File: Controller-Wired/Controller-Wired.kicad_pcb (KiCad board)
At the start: 4 copper layers, 73.5 x 47.5 mm, 33 parts, among them J1 Conn_01x03, J2 Conn_02x20_Odd_Even, J3 Conn_01x06, J4 USB_C_Receptacle, SW1 SW_Push, U1 STM32F103CBTx, U2 AP131-33, U3 USBLC6-2SC6, Y1 Crystal

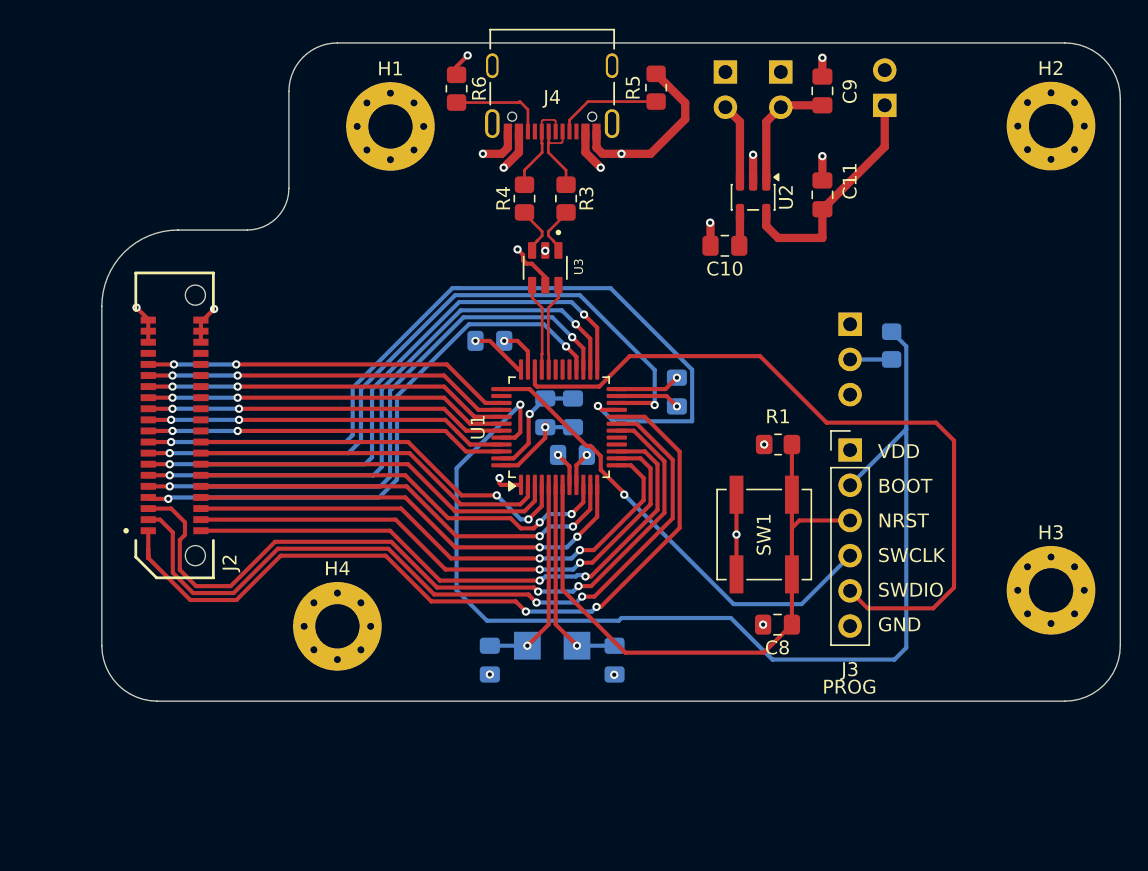
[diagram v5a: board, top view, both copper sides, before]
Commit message: USB connector was giving some net problems, swapped with a different one
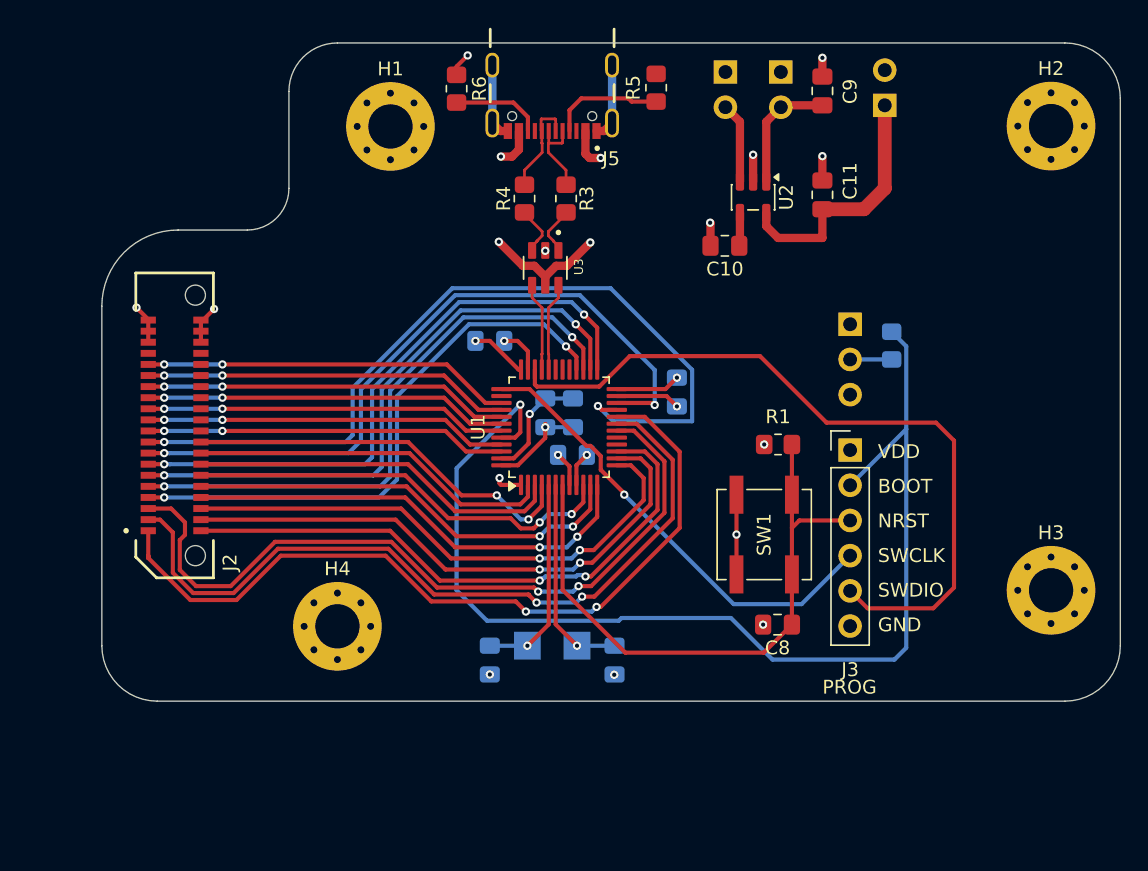
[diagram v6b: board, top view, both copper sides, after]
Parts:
- removed J4: USB_C_Receptacle, Controller:AMPHENOL_12402012E212A
- added J5: USB4105-GF-A, Controller:GCT_USB4105-GF-A, F.Cu at (124.0, 40.1)
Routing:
- net VBUS: track 9.77 -> 15.0 mm, vias 3 -> 4
- net GND: track 51.8 -> 46.8 mm, vias 17 -> 15
- net Net-(JP3-A): track 16.8 -> 18.5 mm
- net D_1-: track 6.95 -> 6.27 mm
- net COL15: track 59.2 -> 58.5 mm
- net Net-(J5-CC1): track 7.63 -> 8.20 mm
